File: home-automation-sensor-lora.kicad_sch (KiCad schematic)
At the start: 90 parts, among them J1 Thermistor, J2 Conn_01x08, J3 Stemma-QT-Connector, J4 USB4105-GF-A_Lizard, J5 3V3-16V, J6 Conn_01x04, Q1 DMN2046U-7, Q2 DMN2046U-7, Q3 DMG3415U-13, U1 LD2985BM33R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

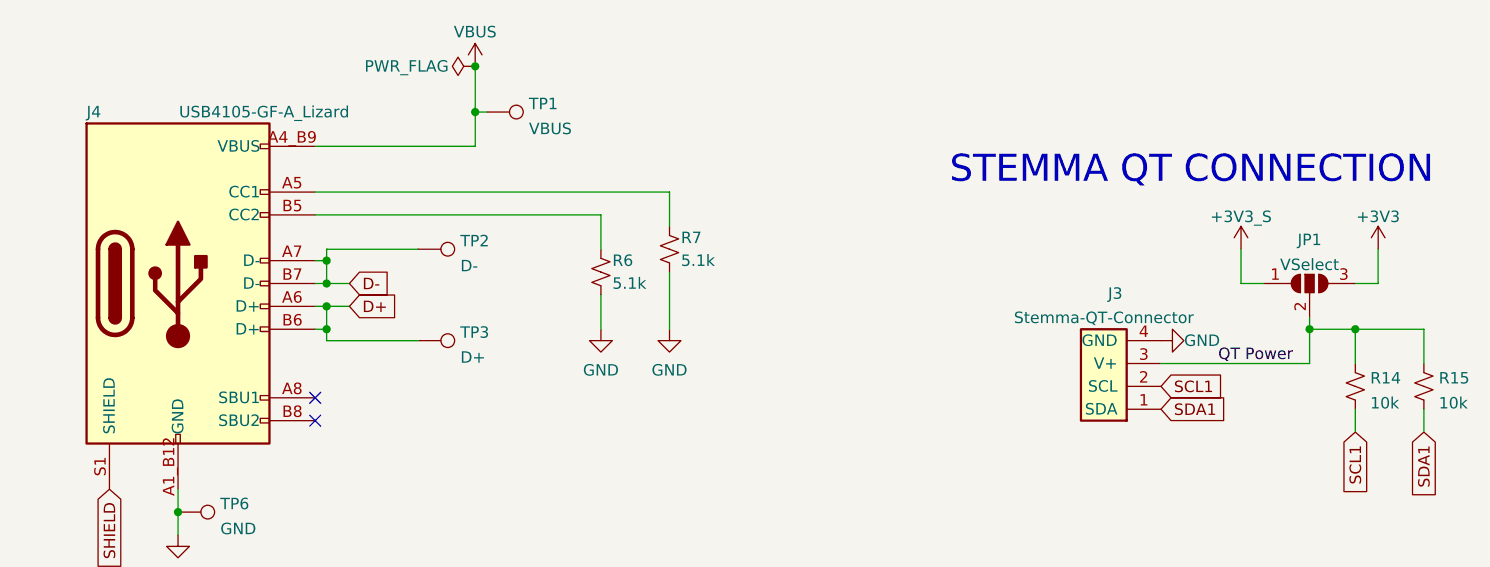
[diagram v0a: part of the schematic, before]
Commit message: Updated RP2040 footprint and updated routing to accommodate it
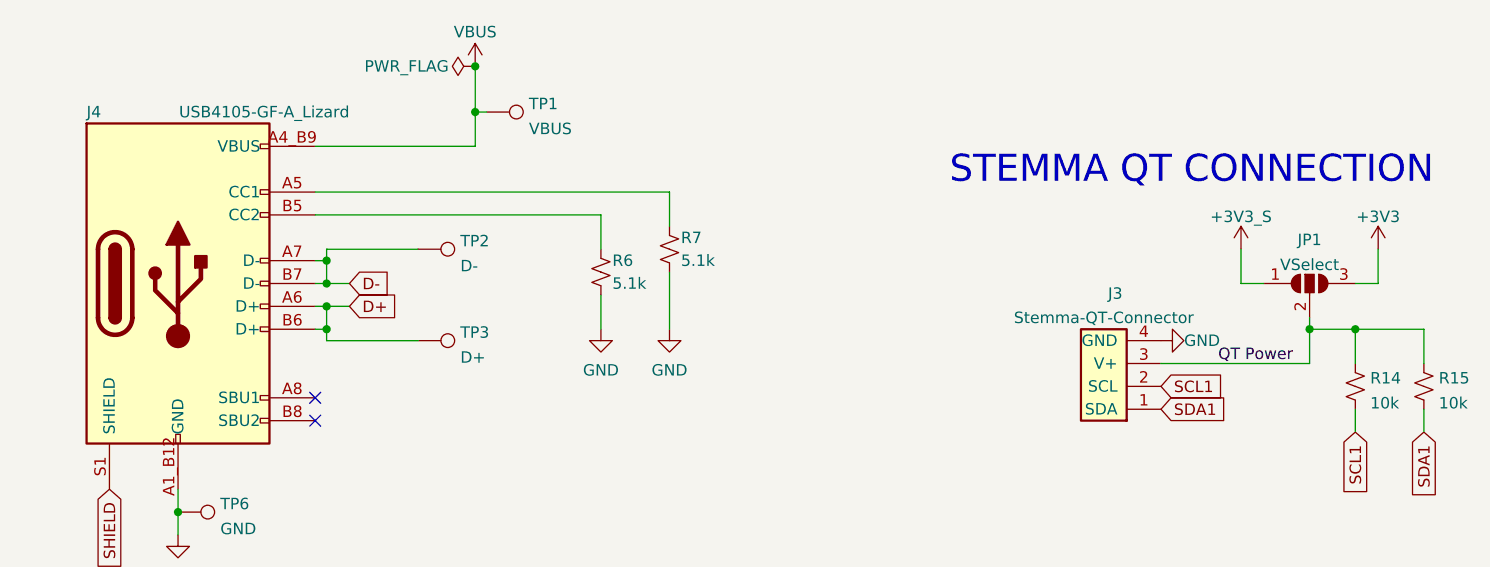
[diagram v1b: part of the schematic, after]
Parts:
- U5: footprint Package_DFN_QFN:QFN-56-1EP_8x8mm_P0.5mm_EP4.5x5.2mm_ThermalVias -> lizard_libs:RP2040_QFN-56

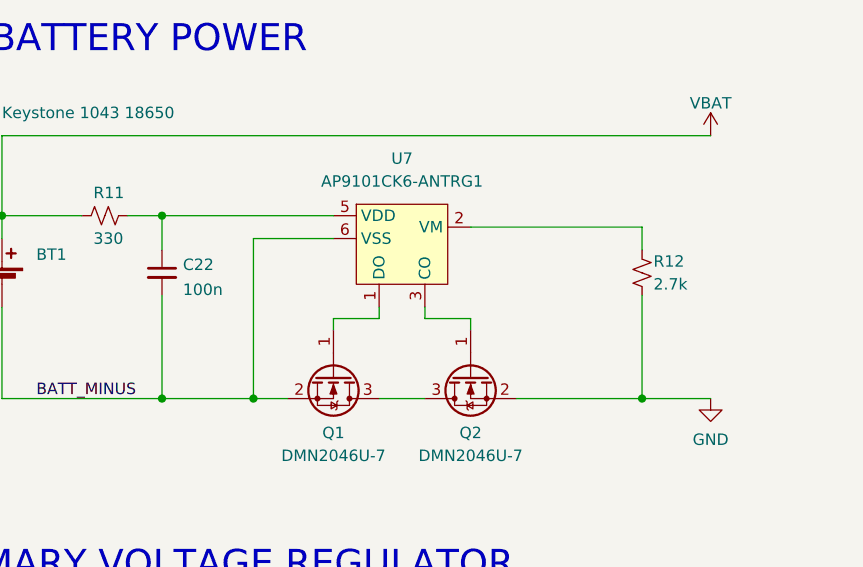
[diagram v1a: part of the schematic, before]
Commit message: Added test points to BMS chip.
Tested BMS functionality and it is not working. It will prevent the battery from being charged at a high voltage, but it will not allow the battery to discharge under normal conditions. Interestingly, attaching 5V to VBUS or VCC while the battery is installed, then removing it, will "kick start" the BMS and allow discharging from the battery.
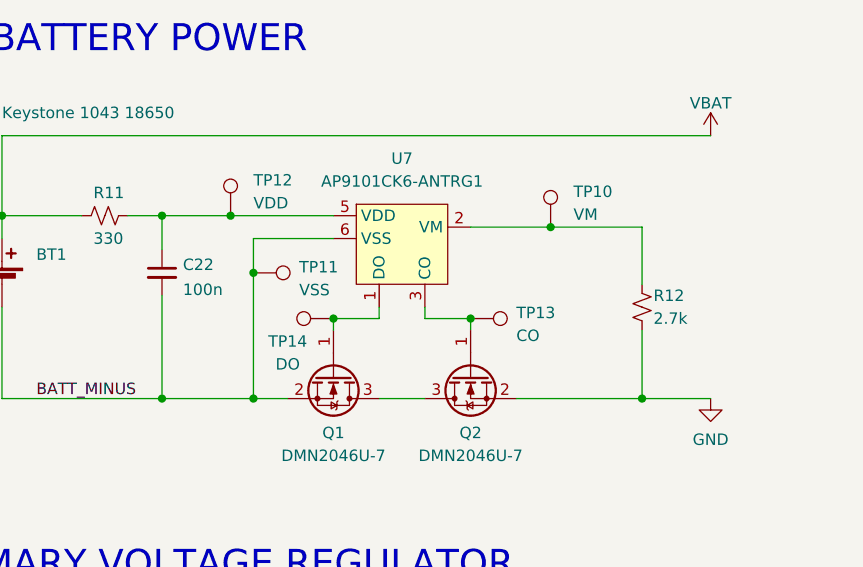
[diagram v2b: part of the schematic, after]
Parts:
- added TP10: VM, lizard_libs:TestPoint_THTPad_1.0x1.0mm_Drill0.5mm-Lizard, symbol Connector:TestPoint
- added TP11: VSS, lizard_libs:TestPoint_THTPad_1.0x1.0mm_Drill0.5mm-Lizard, symbol Connector:TestPoint
- added TP12: VDD, lizard_libs:TestPoint_THTPad_1.0x1.0mm_Drill0.5mm-Lizard, symbol Connector:TestPoint
- added TP13: CO, lizard_libs:TestPoint_THTPad_1.0x1.0mm_Drill0.5mm-Lizard, symbol Connector:TestPoint
- added TP14: DO, lizard_libs:TestPoint_THTPad_1.0x1.0mm_Drill0.5mm-Lizard, symbol Connector:TestPoint
- H1, H2, H3, H4: footprint lizard_libs:MountingHole_2.5mm_Mask -> lizard_libs:Lizard_MountingHole_3.5mm
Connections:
- net BATT_MINUS: now also TP11.1
- net at C22.1, R11.1, U7.5 (VDD): now also TP12.1
- net at R12.1, U7.2 (VM): now also TP10.1
- net at Q2.1 (G), U7.3 (CO): now also TP13.1
- net at Q1.1 (G), U7.1 (DO): now also TP14.1
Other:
- moved on the sheet: R12
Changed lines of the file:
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@@
   (junction (at 55.88 119.38) (diameter 0) (color 0 0 0 0)
   )
+  (junction (at 52.07 43.18) (diameter 0) (color 0 0 0 0)
+  )
   (junction (at 373.38 50.8) (diameter 0) (color 0 0 0 0)
   )
@@
   (junction (at 95.25 161.29) (diameter 0) (color 0 0 0 0)
   )
+  (junction (at 49.53 36.83) (diameter 0) (color 0 0 0 0)
+  )
   (junction (at 127 50.8) (diameter 0) (color 0 0 0 0)
   )
+  (junction (at 85.09 38.1) (diameter 0) (color 0 0 0 0)
+  )
   (junction (at 346.71 50.8) (diameter 0) (color 0 0 0 0)
   )
@@
   (junction (at 158.75 181.61) (diameter 0) (color 0 0 0 0)
   )
+  (junction (at 76.2 48.26) (diameter 0) (color 0 0 0 0)
+  )
   (junction (at 127 36.83) (diameter 0) (color 0 0 0 0)
   )
@@
   (junction (at 274.32 107.95) (diameter 0) (color 0 0 0 0)
   )
+  (junction (at 60.96 48.26) (diameter 0) (color 0 0 0 0)
+  )
   (junction (at 24.13 36.83) (diameter 0) (color 0 0 0 0)
   )
@@
     (stroke (width 0) (type default))
   )
-  (wire (pts (xy 41.91 36.83) (xy 60.96 36.83))
+  (wire (pts (xy 41.91 36.83) (xy 49.53 36.83))
     (stroke (width 0) (type default))
   )
@@
     (stroke (width 0) (type default))
   )
-  (wire (pts (xy 95.25 38.1) (xy 95.25 40.64))
+  (wire (pts (xy 95.25 38.1) (xy 95.25 44.45))
     (stroke (width 0) (type default))
   )
@@
     (stroke (width 0) (type default))
   )
+  (wire (pts (xy 52.07 43.18) (xy 52.07 57.15))
+    (stroke (width 0) (type default))
+  )
   (wire (pts (xy 227.33 99.06) (xy 227.33 104.14))
     (stroke (width 0) (type default))
@@
     (stroke (width 0) (type default))
   )
+  (wire (pts (xy 49.53 36.83) (xy 60.96 36.83))
+    (stroke (width 0) (type default))
+  )
   (wire (pts (xy 285.75 44.45) (xy 285.75 49.53))
     (stroke (width 0) (type default))
@@
     (stroke (width 0) (type default))
   )
-  (wire (pts (xy 52.07 39.37) (xy 52.07 57.15))
+  (wire (pts (xy 52.07 39.37) (xy 52.07 43.18))
     (stroke (width 0) (type default))
   )
@@
     (stroke (width 0) (type default))
   )
-  (wire (pts (xy 76.2 38.1) (xy 95.25 38.1))
+  (wire (pts (xy 76.2 38.1) (xy 85.09 38.1))
     (stroke (width 0) (type default))
   )
@@
     (stroke (width 0) (type default))
   )
+  (wire (pts (xy 85.09 38.1) (xy 95.25 38.1))
+    (stroke (width 0) (type default))
+  )
   (wire (pts (xy 162.56 179.07) (xy 162.56 181.61))
     (stroke (width 0) (type default))
@@
     (stroke (width 0) (type default))
   )
-  (wire (pts (xy 95.25 45.72) (xy 95.25 57.15))
+  (wire (pts (xy 95.25 49.53) (xy 95.25 57.15))
     (stroke (width 0) (type default))
   )
@@
     )
   )
-  (symbol (lib_id "Device:R_Small_US") (at 95.25 43.18 0) (unit 1)
+  (symbol (lib_id "Device:R_Small_US") (at 95.25 46.99 0) (unit 1)
     (in_bom yes) (on_board yes) (dnp no)
-    (property "Reference" "R12" (at 96.52 41.91 0)
+    (property "Reference" "R12" (at 96.52 45.72 0)
       (effects (font (size 1.27 1.27)) (justify left))
     )
-    (property "Value" "2.7k" (at 96.52 44.45 0)
+    (property "Value" "2.7k" (at 96.52 48.26 0)
       (effects (font (size 1.27 1.27)) (justify left))
     )
-    (property "Footprint" "lizard_libs:R_0603_Lizard" (at 95.25 43.18 0)
+    (property "Footprint" "lizard_libs:R_0603_Lizard" (at 95.25 46.99 0)
       (effects (font (size 1.27 1.27)) hide)
     )
-    (property "Datasheet" "~" (at 95.25 43.18 0)
+    (property "Datasheet" "~" (at 95.25 46.99 0)
       (effects (font (size 1.27 1.27)) hide)
     )
@@
     )
   )
+  (symbol (lib_id "Connector:TestPoint") (at 76.2 48.26 270) (unit 1)
+    (in_bom yes) (on_board yes) (dnp no) (fields_autoplaced)
+    (property "Reference" "TP13" (at 81.28 47.625 90)
+      (effects (font (size 1.27 1.27)) (justify left))
+    )
+    (property "Value" "CO" (at 81.28 50.165 90)
+      (effects (font (size 1.27 1.27)) (justify left))
+    )
+    (property "Footprint" "lizard_libs:TestPoint_THTPad_1.0x1.0mm_Drill0.5mm-Lizard" (at 76.2 53.34 0)
+      (effects (font (size 1.27 1.27)) hide)
+    )
+    (property "Datasheet" "~" (at 76.2 53.34 0)
+      (effects (font (size 1.27 1.27)) hide)
+    )
+    (pin "1")
+    (instances
+      (project "home-automation-sensor-lora"
+        (path "/e63e39d7-6ac0-4ffd-8aa3-1841a4541b55"
+          (reference "TP13") (unit 1)
+        )
+      )
+    )
+  )
   (symbol (lib_id "power:GND") (at 55.88 123.19 0) (unit 1)
     (in_bom yes) (on_board yes) (dnp no) (fields_autoplaced)
@@
       (effects (font (size 1.27 1.27)))
     )
-    (property "Footprint" "lizard_libs:MountingHole_2.5mm_Mask" (at 293.37 247.65 0)
+    (property "Footprint" "lizard_libs:Lizard_MountingHole_3.5mm" (at 293.37 247.65 0)
       (effects (font (size 1.27 1.27)) hide)
     )
@@
       (effects (font (size 1.27 1.27)))
     )
-    (property "Footprint" "lizard_libs:MountingHole_2.5mm_Mask" (at 293.37 260.35 0)
+    (property "Footprint" "lizard_libs:Lizard_MountingHole_3.5mm" (at 293.37 260.35 0)
       (effects (font (size 1.27 1.27)) hide)
     )
@@
     )
   )
+  (symbol (lib_id "Connector:TestPoint") (at 52.07 43.18 270) (unit 1)
+    (in_bom yes) (on_board yes) (dnp no) (fields_autoplaced)
+    (property "Reference" "TP11" (at 57.15 42.545 90)
+      (effects (font (size 1.27 1.27)) (justify left))
+    )
+    (property "Value" "VSS" (at 57.15 45.085 90)
+      (effects (font (size 1.27 1.27)) (justify left))
+    )
+    (property "Footprint" "lizard_libs:TestPoint_THTPad_1.0x1.0mm_Drill0.5mm-Lizard" (at 52.07 48.26 0)
+      (effects (font (size 1.27 1.27)) hide)
+    )
+    (property "Datasheet" "~" (at 52.07 48.26 0)
+      (effects (font (size 1.27 1.27)) hide)
+    )
+    (pin "1")
+    (instances
+      (project "home-automation-sensor-lora"
+        (path "/e63e39d7-6ac0-4ffd-8aa3-1841a4541b55"
+          (reference "TP11") (unit 1)
+        )
+      )
+    )
+  )
   (symbol (lib_id "Device:R_Small_US") (at 280.67 90.17 90) (unit 1)
     (in_bom yes) (on_board yes) (dnp no)
@@
     )
   )
+  (symbol (lib_id "Connector:TestPoint") (at 49.53 36.83 0) (unit 1)
+    (in_bom yes) (on_board yes) (dnp no) (fields_autoplaced)
+    (property "Reference" "TP12" (at 52.07 32.893 0)
+      (effects (font (size 1.27 1.27)) (justify left))
+    )
+    (property "Value" "VDD" (at 52.07 35.433 0)
+      (effects (font (size 1.27 1.27)) (justify left))
+    )
+    (property "Footprint" "lizard_libs:TestPoint_THTPad_1.0x1.0mm_Drill0.5mm-Lizard" (at 54.61 36.83 0)
+      (effects (font (size 1.27 1.27)) hide)
+    )
+    (property "Datasheet" "~" (at 54.61 36.83 0)
+      (effects (font (size 1.27 1.27)) hide)
+    )
+    (pin "1")
+    (instances
+      (project "home-automation-sensor-lora"
+        (path "/e63e39d7-6ac0-4ffd-8aa3-1841a4541b55"
+          (reference "TP12") (unit 1)
+        )
+      )
+    )
+  )
   (symbol (lib_id "power:PWR_FLAG") (at 69.85 105.41 0) (unit 1)
     (in_bom yes) (on_board yes) (dnp no)
@@
       (effects (font (size 1.27 1.27)))
     )
-    (property "Footprint" "lizard_libs:MountingHole_2.5mm_Mask" (at 293.37 254 0)
+    (property "Footprint" "lizard_libs:Lizard_MountingHole_3.5mm" (at 293.37 254 0)
       (effects (font (size 1.27 1.27)) hide)
     )
@@
       (effects (font (size 1.27 1.27)))
     )
-    (property "Footprint" "lizard_libs:MountingHole_2.5mm_Mask" (at 293.37 241.3 0)
+    (property "Footprint" "lizard_libs:Lizard_MountingHole_3.5mm" (at 293.37 241.3 0)
       (effects (font (size 1.27 1.27)) hide)
     )
@@
     )
   )
+  (symbol (lib_id "Connector:TestPoint") (at 60.96 48.26 90) (unit 1)
+    (in_bom yes) (on_board yes) (dnp no)
+    (property "Reference" "TP14" (at 55.88 50.8 90)
+      (effects (font (size 1.27 1.27)))
+    )
+    (property "Value" "DO" (at 55.88 53.34 90)
+      (effects (font (size 1.27 1.27)))
+    )
+    (property "Footprint" "lizard_libs:TestPoint_THTPad_1.0x1.0mm_Drill0.5mm-Lizard" (at 60.96 43.18 0)
+      (effects (font (size 1.27 1.27)) hide)
+    )
+    (property "Datasheet" "~" (at 60.96 43.18 0)
+      (effects (font (size 1.27 1.27)) hide)
+    )
+    (pin "1")
+    (instances
+      (project "home-automation-sensor-lora"
+        (path "/e63e39d7-6ac0-4ffd-8aa3-1841a4541b55"
+          (reference "TP14") (unit 1)
+        )
+      )
+    )
+  )
   (symbol (lib_id "lizard_lib:+3V3_S") (at 364.49 176.53 0) (unit 1)
     (in_bom yes) (on_board yes) (dnp no) (fields_autoplaced)
@@
         )
       )
+    )
+  )
+  (symbol (lib_id "Connector:TestPoint") (at 85.09 38.1 0) (unit 1)
+    (in_bom yes) (on_board yes) (dnp no) (fields_autoplaced)
+    (property "Reference" "TP10" (at 87.63 34.163 0)
+      (effects (font (size 1.27 1.27)) (justify left))
+    )
+    (property "Value" "VM" (at 87.63 36.703 0)
+      (effects (font (size 1.27 1.27)) (justify left))
+    )
+    (property "Footprint" "lizard_libs:TestPoint_THTPad_1.0x1.0mm_Drill0.5mm-Lizard" (at 90.17 38.1 0)
+      (effects (font (size 1.27 1.27)) hide)
+    )
+    (property "Datasheet" "~" (at 90.17 38.1 0)
+      (effects (font (size 1.27 1.27)) hide)
+    )
+    (pin "1")
+    (instances
+      (project "home-automation-sensor-lora"
+        (path "/e63e39d7-6ac0-4ffd-8aa3-1841a4541b55"
+          (reference "TP10") (unit 1)
+        )
+      )

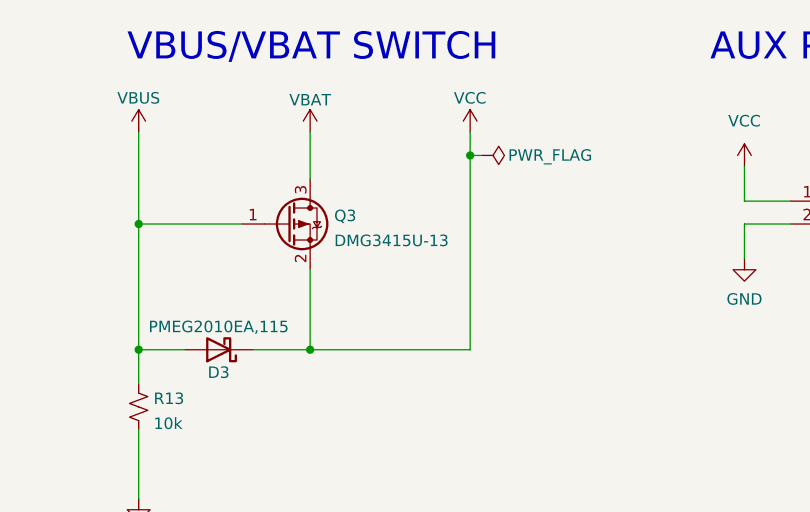
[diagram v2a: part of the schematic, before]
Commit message: Adjusted power planes around BMS
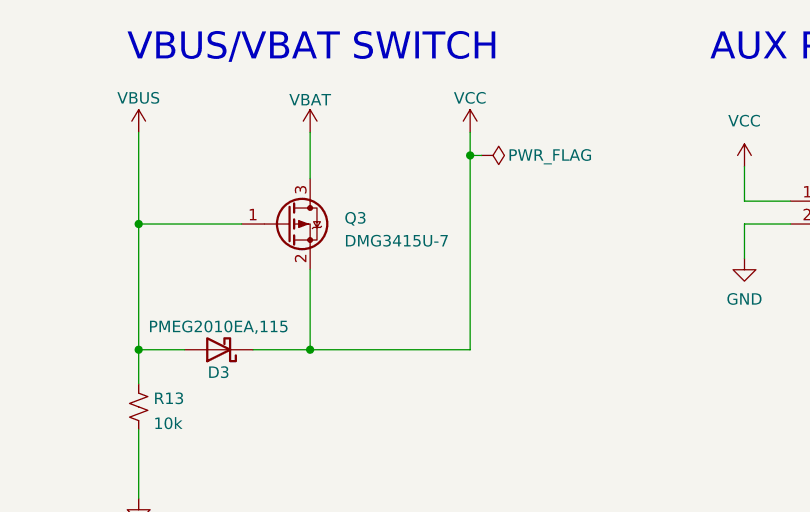
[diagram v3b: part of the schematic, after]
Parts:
- Q3: value DMG3415U-13 -> DMG3415U-7
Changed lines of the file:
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@@
   (symbol (lib_id "lizard_lib:DMG3415U-13") (at 143.51 36.83 0) (unit 1)
     (in_bom yes) (on_board yes) (dnp no) (fields_autoplaced)
-    (property "Reference" "Q3" (at 148.717 35.9215 0)
+    (property "Reference" "Q3" (at 149.86 36.195 0)
       (effects (font (size 1.27 1.27)) (justify left))
     )
-    (property "Value" "DMG3415U-13" (at 148.717 38.6966 0)
+    (property "Value" "DMG3415U-7" (at 149.86 38.735 0)
       (effects (font (size 1.27 1.27)) (justify left))
     )

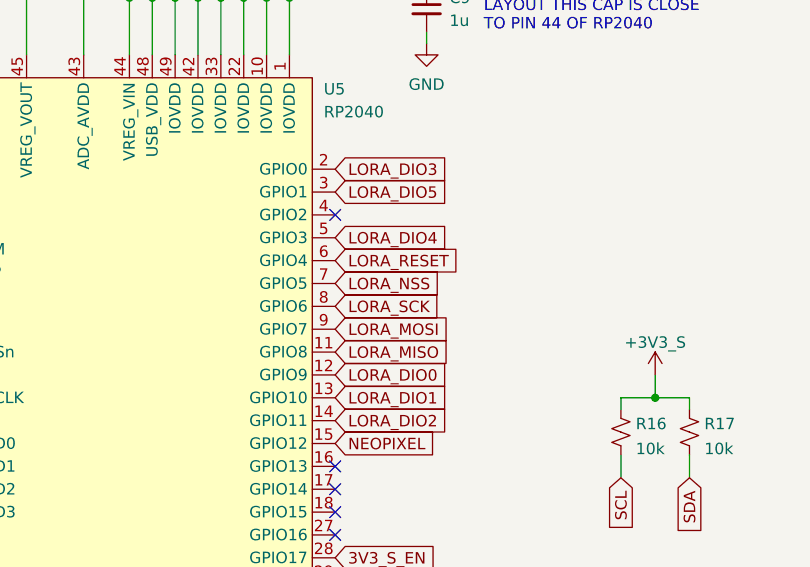
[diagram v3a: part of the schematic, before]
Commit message: Moved LORA_MISO to GPIO4 and LORA_RESET to GPIO2
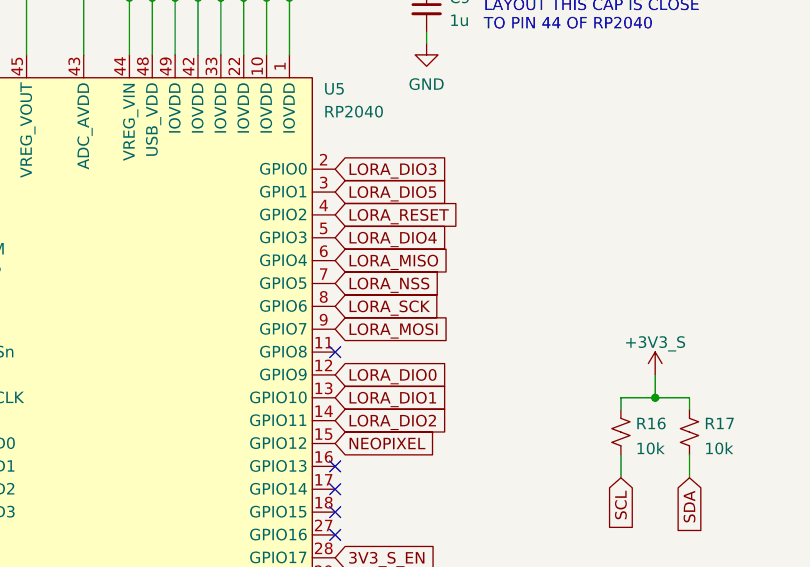
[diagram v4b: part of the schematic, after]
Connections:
- net LORA_MISO: now also U5.6 (GPIO4); no longer U5.11 (GPIO8)
- net LORA_RESET: now also U5.4 (GPIO2); no longer U5.6 (GPIO4)
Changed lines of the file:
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@@
   (no_connect (at 48.26 243.84))
   (no_connect (at 410.21 213.36))
-  (no_connect (at 340.36 92.71))
+  (no_connect (at 340.36 107.95))
   (wire (pts (xy 298.45 34.29) (xy 298.45 49.53))
     (stroke (width 0) (type default))
@@
     )
   )
-  (global_label "LORA_RESET" (shape input) (at 340.36 97.79 0) (fields_autoplaced)
-    (effects (font (size 1.27 1.27)) (justify left))
-    (property "Intersheetrefs" "${INTERSHEET_REFS}" (at 354.2031 97.7106 0)
+  (global_label "LORA_RESET" (shape input) (at 340.36 92.71 0) (fields_autoplaced)
+    (effects (font (size 1.27 1.27)) (justify left))
+    (property "Intersheetrefs" "${INTERSHEET_REFS}" (at 354.2031 92.6306 0)
       (effects (font (size 1.27 1.27)) (justify left) hide)
     )
@@
     )
   )
-  (global_label "LORA_MISO" (shape input) (at 340.36 107.95 0) (fields_autoplaced)
-    (effects (font (size 1.27 1.27)) (justify left))
-    (property "Intersheetrefs" "${INTERSHEET_REFS}" (at 353.0541 107.8706 0)
-      (effects (font (size 1.27 1.27)) (justify left) hide)
-    )
+  (global_label "LORA_MISO" (shape input) (at 340.36 97.79 0) (fields_autoplaced)
+    (effects (font (size 1.27 1.27)) (justify left))
+    (property "Intersheetrefs" "${INTERSHEET_REFS}" (at 353.0541 97.7106 0)
+      (effects (font (size 1.27 1.27)) (justify left) hide)
+    )
